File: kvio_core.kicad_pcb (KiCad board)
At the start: 6 copper layers, 93 x 30 mm, 261 parts, among them J1001 12-pin_FFC_(SFV12R), J1301 USB3_B_Micro, J301 Conn_01x06_Male, J401 12-pin_FFC_(SFV12R), J801 12-pin_FFC_(SFV12R), J901 12-pin_FFC_(SFV12R), U1001 IP4254CZ8-4-TTL, U1002 EMI8143, U101 xc7a100t-csg324, U1101 AR0135CS, U1201 MT41J128M16JT-125:K, U1301 FT601Q, U1302 EMI8143, U1401 AR0135CS, U201 FAN53541, U202 FAN53541, U203 FAN53541, U204 FAN53541, U301 MX25L3233F, U302 MAX809, U401 EMI8143, U402 IP4254CZ8-4-TTL, U801 IP4254CZ8-4-TTL, U802 EMI8143, U901 IP4254CZ8-4-TTL, U902 EMI8143, Y1301 Crystal_GND24_Small

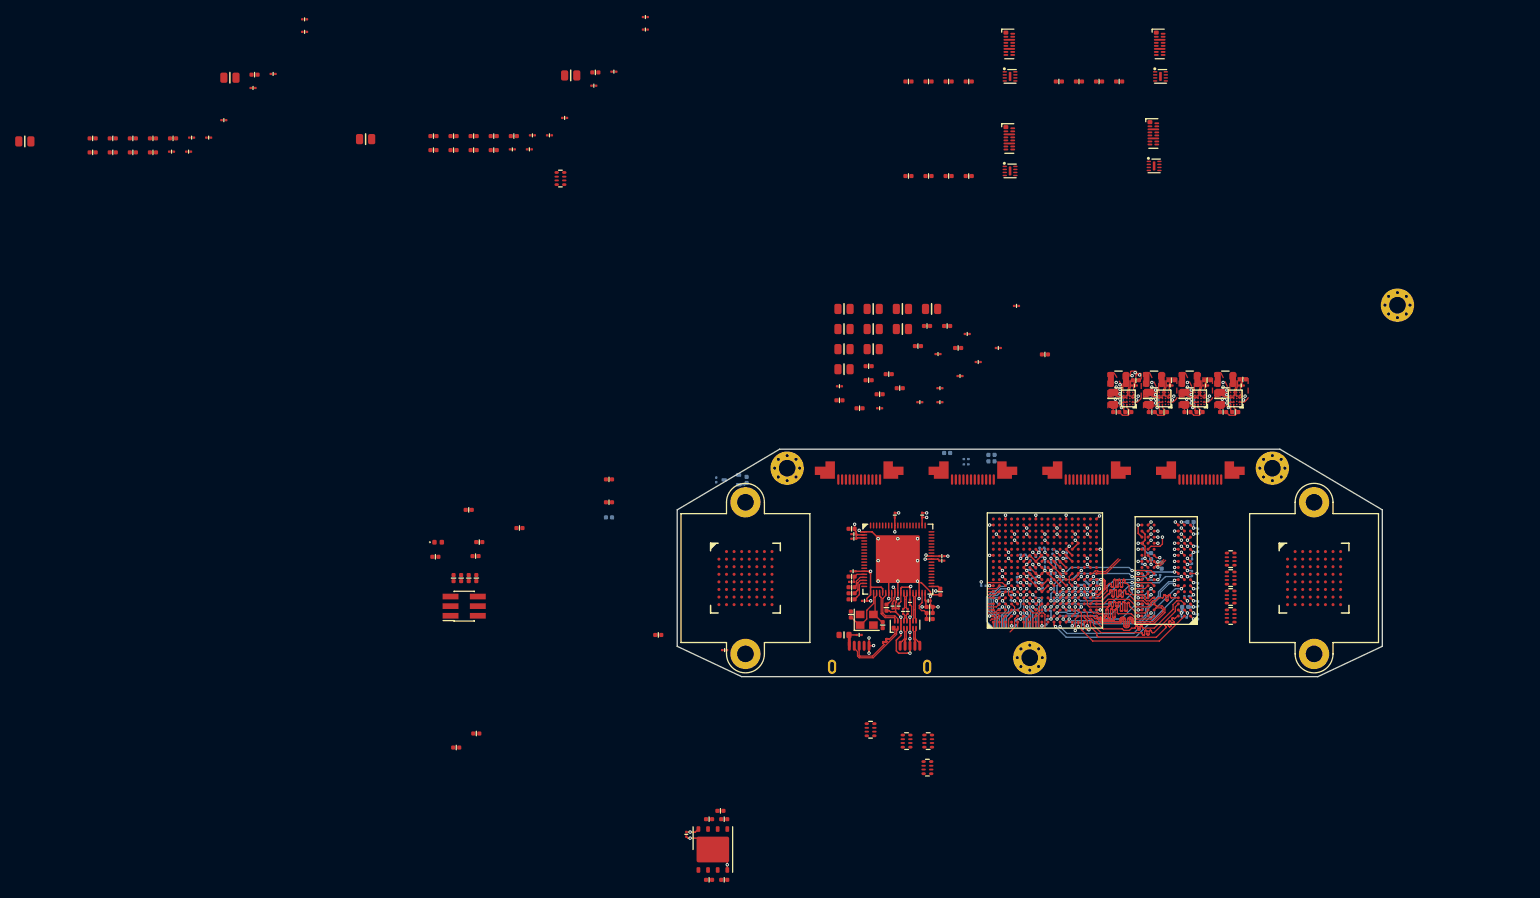
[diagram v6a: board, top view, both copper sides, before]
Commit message: USB3 FIFO layout done, some testing with camera connectors
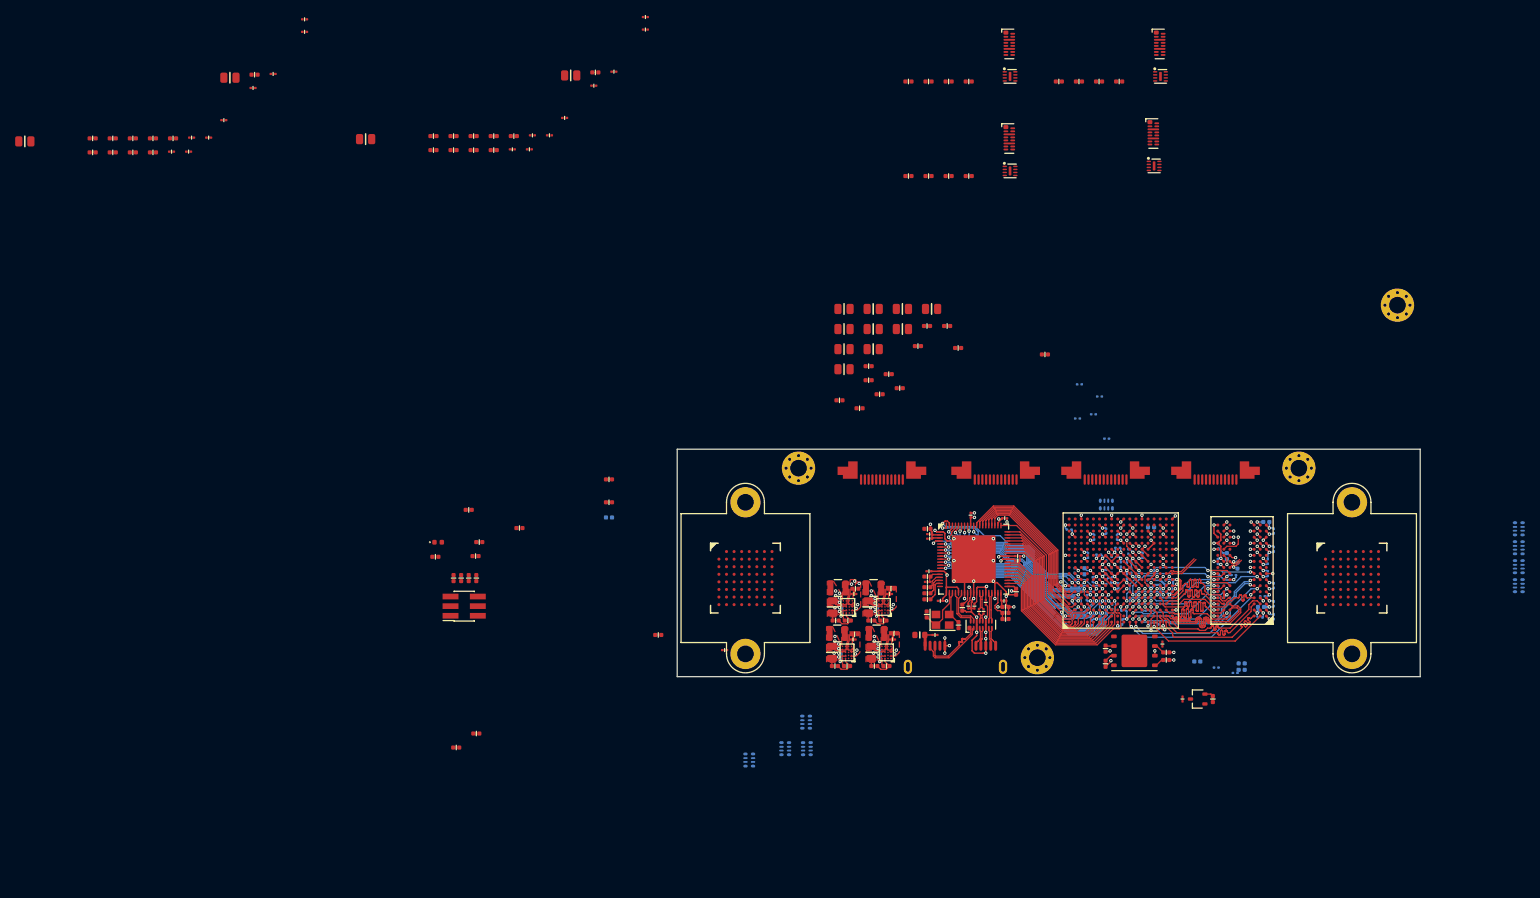
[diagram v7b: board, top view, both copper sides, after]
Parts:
- added R304: 100, passive:R_0402, B.Cu at (210.5, 95.3)
- C223, C224, C229, C230, C234, C235, C236, C243, C244, C251, C252, R301, RN101, RN1101, RN1102, RN1103, RN1104, RN1401, RN1402, RN1403, RN1404: moved to B.Cu
- C302, R310, U302: moved to F.Cu
- U301: value MX25L3233F -> MX25L6433F
- moved RN101 83.9 mm to (204.6, 92.3), turned to 270 degrees
- moved C302 68.0 mm to (214.7, 118.0), turned to 90 degrees
- moved R310 68.0 mm to (218.7, 118.0), turned to 90 degrees
- moved U302 68.0 mm to (216.7, 118.0)
- moved C301 67.6 mm to (212.0, 110.7)
- moved R314 64.2 mm to (212.5, 111.8)
- moved R311 62.0 mm to (212.5, 112.8)
- moved U301 61.5 mm to (208.3, 111.6), turned to 0 degrees
- moved R312 60.5 mm to (204.5, 111.3), turned to 90 degrees
- moved R313 57.8 mm to (204.5, 113.3), turned to 90 degrees
- moved R301 57.5 mm to (201.7, 101.1), turned to 90 degrees
- moved C280 57.3 mm to (171.4, 109.4)
- moved C281 57.3 mm to (171.2, 110.1)
- moved C282 57.3 mm to (168.4, 111.8)
- moved L204 57.3 mm to (169.1, 109.3)
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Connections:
- C203 pad 1: +3V3 -> +1V8
- C207 pad 1: +3V3 -> +1V8
- C212 pad 1: +3V3 -> +1V8
- C217 pad 1: +3V3 -> +1V8
- C223 pad 1: +3V3 -> +1V8
- C229 pad 1: +3V3 -> +1V8
- C235 pad 1: +3V3 -> +1V8
- C243 pad 1: +3V3 -> +1V8
- C251 pad 1: +3V3 -> +1V8
- R1101 pad 1: /CAM_RESET -> /CAM1_RESET
- R1404 pad 1: /CAM_RESET -> /CAM0_RESET
- RN101 pad 1: /CAM_CLK -> /CAM0_CLK_P
- RN101 pad 2: /CAM_CLK -> /CAM1_CLK_P
- U101 pad A11: Net-(U101-PadA11) -> /CAM0_D3
- U101 pad A13: Net-(U101-PadA13) -> /CAM0_FV
- U101 pad A14: Net-(U101-PadA14) -> /CAM0_LV
- U101 pad A15: Net-(U101-PadA15) -> /CAM0_D10
- U101 pad A16: Net-(U101-PadA16) -> /CAM0_D11
- U101 pad A17: +3V3 -> +1V8
- U101 pad A18: Net-(U101-PadA18) -> /CAM0_FLASH
- U101 pad B11: Net-(U101-PadB11) -> /CAM0_D2
- U101 pad B12: Net-(U101-PadB12) -> /CAM0_D1
- U101 pad B13: Net-(U101-PadB13) -> /CAM1_RESET
- U101 pad B14: Net-(U101-PadB14) -> /CAM0_D0
- U101 pad B16: Net-(U101-PadB16) -> /CAM0_D8
- U101 pad B17: Net-(U101-PadB17) -> /CAM0_D9
- U101 pad B18: Net-(U101-PadB18) -> /CAM0_TRIGGER
- U101 pad C12: Net-(U101-PadC12) -> /CAM0_RESET
- U101 pad C13: +3V3 -> +1V8
- U101 pad C15: Net-(U101-PadC15) -> /CAM1_PIXCLK
- U101 pad C16: Net-(U101-PadC16) -> /CAM1_TRIGGER
- U101 pad C17: Net-(U101-PadC17) -> /CAM1_FLASH
- U101 pad D12: Net-(U101-PadD12) -> /CAM0_D6
- U101 pad D13: Net-(U101-PadD13) -> /CAM0_D7
- U101 pad D15: Net-(U101-PadD15) -> /CAM0_PIXCLK
- U101 pad D16: +3V3 -> +1V8
- U101 pad D17: Net-(U101-PadD17) -> /CAM1_D7
- U101 pad D18: Net-(U101-PadD18) -> /CAM1_SCLK
- U101 pad E15: Net-(U101-PadE15) -> /CAM0_SDATA
- U101 pad E16: Net-(U101-PadE16) -> /CAM0_SCLK
- U101 pad E17: Net-(U101-PadE17) -> /CAM1_D6
- U101 pad E18: Net-(U101-PadE18) -> /CAM1_SDATA
- U101 pad F13: Net-(U101-PadF13) -> /CAM0_D4
- U101 pad F14: Net-(U101-PadF14) -> /CAM0_D5
- U101 pad F15: Net-(U101-PadF15) -> /CAM1_D2
- U101 pad F16: Net-(U101-PadF16) -> /CAM1_D3
- U101 pad F18: Net-(U101-PadF18) -> /CAM0_CLK_P
- U101 pad G14: Net-(U101-PadG14) -> /CAM1_D5
- U101 pad G15: +3V3 -> +1V8
- U101 pad G16: Net-(U101-PadG16) -> /CAM1_D1
- U101 pad G17: Net-(U101-PadG17) -> /CAM1_D11
- U101 pad G18: Net-(U101-PadG18) -> /CAM1_CLK_P
- U101 pad H14: Net-(U101-PadH14) -> /CAM1_D4
- U101 pad H15: Net-(U101-PadH15) -> /CAM1_LV
- U101 pad H16: Net-(U101-PadH16) -> /CAM1_D0
- U101 pad H17: Net-(U101-PadH17) -> /CAM1_D10
- U101 pad H18: +3V3 -> +1V8
- U101 pad J13: Net-(U101-PadJ13) -> /CAM1_D9
- U101 pad J14: Net-(U101-PadJ14) -> /CAM1_FV
- U101 pad K13: Net-(U101-PadK13) -> /CAM1_D8
- U101 pad K14: +3V3 -> +1V8
- U101 pad L18: /CAM0_D1 -> Net-(U101-PadL18)
- U101 pad M13: /CAM0_D5 -> Net-(U101-PadM13)
- U101 pad M16: /CAM0_FV -> Net-(U101-PadM16)
- U101 pad M17: /CAM0_LV -> Net-(U101-PadM17)
- U101 pad M18: /CAM0_D2 -> Net-(U101-PadM18)
- U101 pad N14: /CAM0_D8 -> Net-(U101-PadN14)
- U101 pad N15: /CAM0_TRIGGER -> Net-(U101-PadN15)
- U101 pad N16: /CAM0_FLASH -> Net-(U101-PadN16)
- U101 pad N17: /CAM0_D10 -> Net-(U101-PadN17)
- U101 pad P14: /CAM0_D9 -> Net-(U101-PadP14)
- U101 pad P15: /CAM0_PIXCLK -> Net-(U101-PadP15)
- U101 pad P17: /CAM0_SDATA -> Net-(U101-PadP17)
- U101 pad P18: /CAM0_D11 -> Net-(U101-PadP18)
- U101 pad R10: /CAM_RESET -> Net-(U101-PadR10)
- U101 pad R11: /CAM0_D0 -> Net-(U101-PadR11)
- U101 pad R12: /CAM0_D3 -> Net-(U101-PadR12)
- U101 pad R13: /CAM0_D4 -> Net-(U101-PadR13)
- U101 pad R15: /CAM1_PIXCLK -> Net-(U101-PadR15)
- U101 pad R17: /CAM0_SCLK -> Net-(U101-PadR17)
- U101 pad R18: /CAM0_D6 -> Net-(U101-PadR18)
- U101 pad T10: /CAM_CLK -> Net-(U101-PadT10)
- U101 pad T11: /CAM1_D7 -> Net-(U101-PadT11)
- U101 pad T13: /CAM1_FLASH -> Net-(U101-PadT13)
- U101 pad T14: /CAM1_D0 -> Net-(U101-PadT14)
- U101 pad T15: /CAM1_D1 -> Net-(U101-PadT15)
- U101 pad T18: /CAM0_D7 -> Net-(U101-PadT18)
- U101 pad T9: /CAM1_SCLK -> Net-(U101-PadT9)
- U101 pad U11: /CAM1_D8 -> Net-(U101-PadU11)
- U101 pad U12: /CAM1_D9 -> Net-(U101-PadU12)
- U101 pad U13: /CAM1_SDATA -> Net-(U101-PadU13)
- U101 pad U14: /CAM1_LV -> Net-(U101-PadU14)
- U101 pad U16: /CAM1_D5 -> Net-(U101-PadU16)
- U101 pad U17: /CAM1_D3 -> Net-(U101-PadU17)
- U101 pad U18: /CAM1_D4 -> Net-(U101-PadU18)
- U101 pad V10: /CAM1_D11 -> Net-(U101-PadV10)
- U101 pad V11: /CAM1_FV -> Net-(U101-PadV11)
- U101 pad V12: /CAM1_D10 -> Net-(U101-PadV12)
- U101 pad V14: /CAM1_TRIGGER -> Net-(U101-PadV14)
- U101 pad V16: /CAM1_D2 -> Net-(U101-PadV16)
- U101 pad V17: /CAM1_D6 -> Net-(U101-PadV17)
- U1101 pad H8: /CAM_RESET -> /CAM1_RESET
- U1401 pad H8: /CAM_RESET -> /CAM0_RESET
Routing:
- net /USB3 Interface/BE_0: track 0.70 -> 39.2 mm, vias 0 -> 1
- net /USB3 Interface/DATA_28: track 1.67 -> 38.7 mm, vias 0 -> 1
- net /USB3 Interface/RD_N: track 3.93 -> 40.7 mm, vias 0 -> 1
- net /USB3 Interface/BE_1: track 0.70 -> 36.9 mm, vias 0 -> 1
- net /USB3 Interface/WR_N: track 3.15 -> 39.1 mm, vias 0 -> 1
- net /USB3 Interface/DATA_29: track 1.67 -> 37.4 mm, vias 0 -> 1
- net /USB3 Interface/BE_2: track 0.70 -> 35.7 mm, vias 0 -> 1
- net /USB3 Interface/BE_3: track 0.70 -> 34.9 mm, vias 0 -> 1
- net /USB3 Interface/DATA_26: track 2.51 -> 33.6 mm, vias 0 -> 1
- net /USB3 Interface/DATA_31: track 0.70 -> 31.4 mm, vias 0 -> 1
- net /USB3 Interface/DATA_27: track 1.67 -> 32.1 mm, vias 0 -> 1
- net /USB3 Interface/DATA_30: track 1.67 -> 31.7 mm, vias 0 -> 1
- net /USB3 Interface/OE_N: track 4.31 -> 30.4 mm, vias 1 -> 2
- net /USB3 Interface/TXE_N: track 5.93 -> 31.0 mm, vias 1 -> 2
- net /USB3 Interface/RXF_N: track 0.57 -> 25.5 mm, vias 1 -> 2
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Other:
- board size 93 x 30 mm -> 98 x 30 mm

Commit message: Added IMU
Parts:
- added %R: %V, connectors:SOICbiteSmall, F.Cu at (227.5, 114.6)
- added C101: 4.7u, passive:C_0402, F.Cu at (228.0, 123.1)
- added C102: 0.1u, passive:C_0201, F.Cu at (171.9, 93.1)
- added C103: 0.1u, passive:C_0201, F.Cu at (170.6, 93.1)
- added FB101: Ferrite_Bead_Small, passive:R_0402, F.Cu at (228.0, 125.0)
- added R101: 4.7k, passive:R_0402, F.Cu at (230.7, 123.1)
- added U102: ASM330LHH, lga:LGA-14-2.5x3, F.Cu at (171.5, 95.0)
- moved H101 1.50 mm to (165.5, 87.5)
- moved H104 1.50 mm to (228.5, 87.5)
- moved RN101 1.12 mm to (203.6, 92.8), turned to 90 degrees
- moved J401 1.00 mm to (176.0, 86.5)
- moved J801 1.00 mm to (218.0, 86.5)
- moved J901 0.50 mm to (204.0, 86.5)
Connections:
- U101 pad A8: Net-(U101-PadA8) -> /IMU_INT
- U101 pad B8: Net-(U101-PadB8) -> /IMU_SDO
- U101 pad B9: Net-(U101-PadB9) -> /IMU_CS
- U101 pad C9: Net-(U101-PadC9) -> /IMU_SCK
- U101 pad D9: Net-(U101-PadD9) -> /IMU_SDI
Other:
- outline, holes or cut-outs redrawn
